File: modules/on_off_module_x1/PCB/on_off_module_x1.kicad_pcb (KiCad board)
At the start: 2 copper layers, 48 x 63 mm, 30 parts, among them J1 Screw_Terminal_01x02, J2 Conn_01x06_Socket, J3 Conn_01x03_Socket, J4 Screw_Terminal_01x02, J5 Screw_Terminal_01x02, K1 12V 5A, Q1 2N7002H, SW1 SW_SPDT, U1 AMS1117-3.3, U2 ESP-12E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

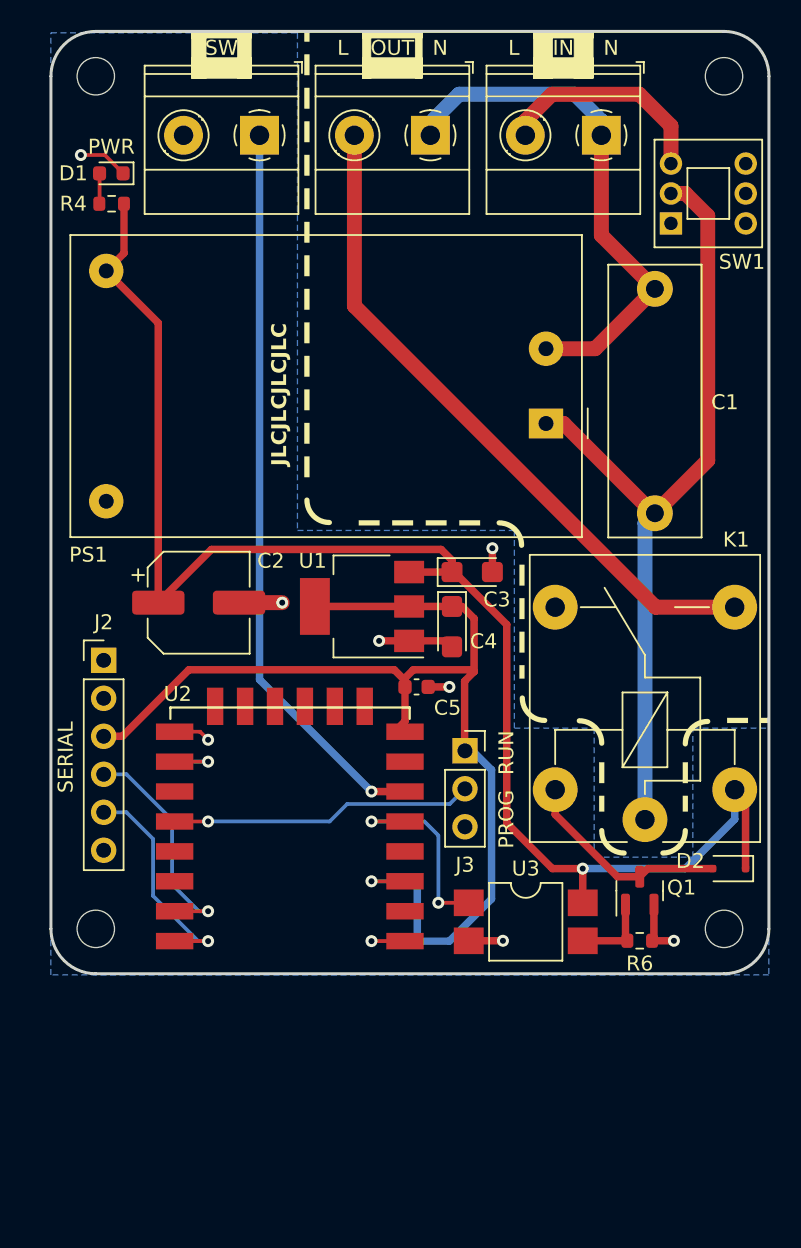
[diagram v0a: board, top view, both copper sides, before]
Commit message: ON-OFF module hardware updated to V2
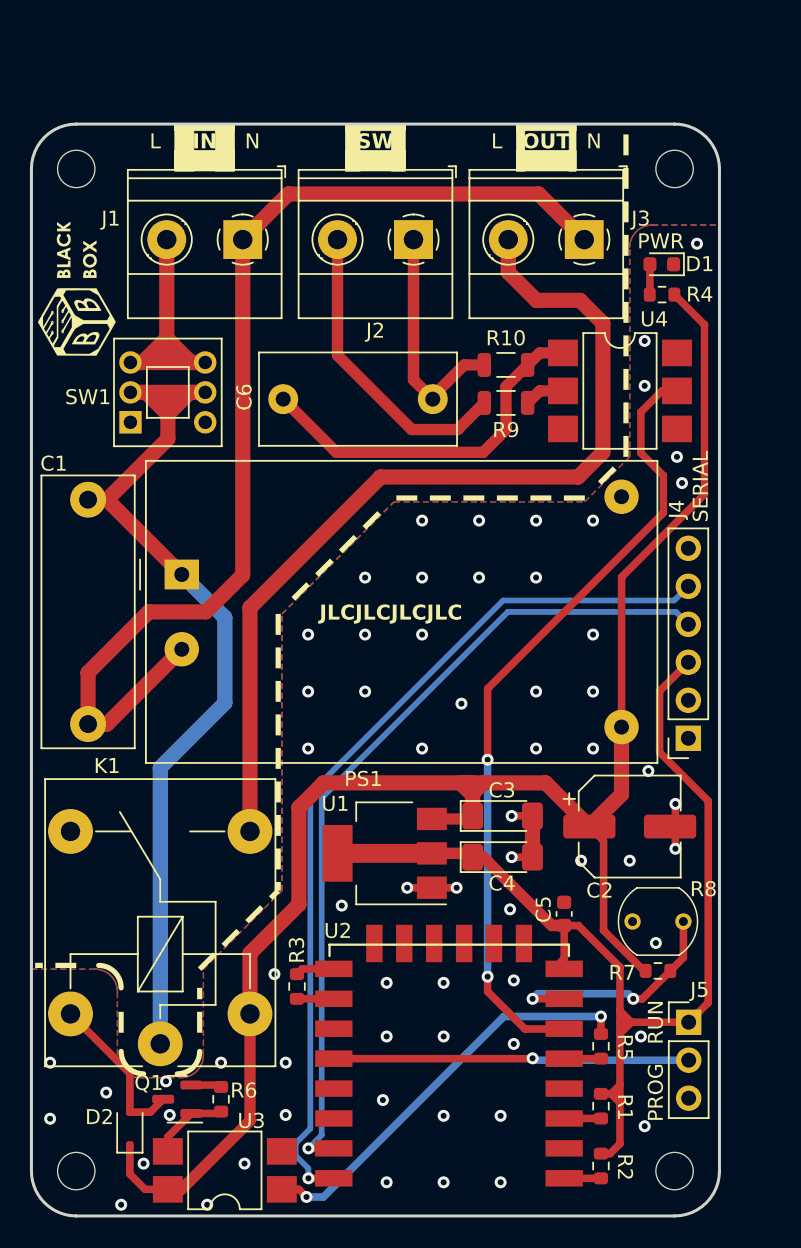
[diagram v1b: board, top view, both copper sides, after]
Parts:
- added C6: 220nF, Alan_Capacitor:CAP_THT_CERAMIC_X2_13x6x12, F.Cu at (152.4, 83.4)
- added G***: LOGO, LOGO, F.Cu at (128.6, 76.1)
- added G***: LOGO, LOGO, B.Cu at (157.0, 123.5)
- added R10: 1M, Alan_Resistor:RES_SMD_1206, F.Cu at (155.8, 81.1)
- added R7: 2.2k, Alan_Resistor:RES_SMD_0603, F.Cu at (166.6, 121.7)
- added R8: 10k, Alan_Sensor:LDR_5_V, F.Cu at (167.4, 118.4)
- added R9: 1k, Alan_Resistor:RES_SMD_1206, F.Cu at (155.8, 83.7)
- added U4: H11AA1, Alan_IC:SMDIP-6_7.62, F.Cu at (164.9, 82.9)
- C1: footprint Capacitor_THT:C_Rect_L18.0mm_W6.0mm_P15.00mm_FKS3_FKP3 -> Alan_Capacitor:CAP_THT_CERAMIC_X2_18x6x15
- C2: footprint Capacitor_SMD:CP_Elec_6.3x7.7 -> Alan_Capacitor:CAP_SMD_ELEC_6.3x7.7
- C3, C4: footprint Capacitor_Tantalum_SMD:CP_EIA-3216-18_Kemet-A -> Alan_Capacitor:CAP_SMD_TANTALUM_CASE-A
- C5: footprint Capacitor_SMD:C_0603_1608Metric -> Alan_Capacitor:CAP_SMD_CERAMIC_0603
- D1: footprint LED_SMD:LED_0603_1608Metric -> Alan_LED:LED_SMD_0603
- D2: footprint Diode_SMD:D_SOD-323F -> Alan_Diode:DIODE_SMD_SOD323F
- J1: footprint TerminalBlock_Phoenix:TerminalBlock_Phoenix_MKDS-1,5-2-5.08_1x02_P5.08mm_Horizontal -> Alan_Connector:CONN_TERMINAL-BLOCK_2P_P5.08
- J2: value Conn_01x06_Socket -> Screw_Terminal_01x02; footprint Connector_PinHeader_2.54mm:PinHeader_1x06_P2.54mm_Vertical -> Alan_Connector:CONN_TERMINAL-BLOCK_2P_P5.08
- J3: value Conn_01x03_Socket -> Screw_Terminal_01x02; footprint Connector_PinSocket_2.54mm:PinSocket_1x03_P2.54mm_Vertical -> Alan_Connector:CONN_TERMINAL-BLOCK_2P_P5.08
- J4: value Screw_Terminal_01x02 -> Conn_01x06_Socket; footprint TerminalBlock_Phoenix:TerminalBlock_Phoenix_MKDS-1,5-2-5.08_1x02_P5.08mm_Horizontal -> Alan_Connector:CONN_SOCKET-HEADER_1x06_V
- J5: value Screw_Terminal_01x02 -> Conn_01x03_Socket; footprint TerminalBlock_Phoenix:TerminalBlock_Phoenix_MKDS-1,5-2-5.08_1x02_P5.08mm_Horizontal -> Alan_Connector:CONN_PIN-HEADER_1x03_V
- K1: footprint Relay_THT:Relay_SPDT_Finder_36.11 -> Alan_Relay:RELAY_SPDT_FINDER_36.11
- PS1: footprint Converter_ACDC:Converter_ACDC_HiLink_HLK-PMxx -> Alan_Module:HILINK_HLK-PMxx
- Q1: footprint Package_TO_SOT_SMD:SOT-23 -> Alan_Transistor:SOT-23
- R1, R2, R3, R5: footprint Resistor_SMD:R_0603_1608Metric -> Alan_Resistor:RES_SMD_0603; moved to F.Cu
- R4, R6: footprint Resistor_SMD:R_0603_1608Metric -> Alan_Resistor:RES_SMD_0603
- SW1: footprint MyLibrary:Toggle_Switch_SelfLocking_7x7 -> Alan_Switches:SW_TOGGLE_DPDT_THT_7x7
- U1: footprint Package_TO_SOT_SMD:SOT-223-3_TabPin2 -> Alan_IC:SOT-223-3_TAB2
- U2: footprint ESP8266:ESP-12E_SMD -> Alan_Module:MOD_ESP-12E
- U3: footprint Package_DIP:SMDIP-4_W7.62mm -> Alan_IC:SMDIP-4_7.62
- moved J5 61.8 mm to (169.5, 125.1), turned to 0 degrees
- moved J4 49.5 mm to (169.5, 106.1)
- moved D2 43.7 mm to (132.1, 132.2), turned to 90 degrees
- moved SW1 38.5 mm to (134.7, 83.0)
- moved R4 38.1 mm to (168.5, 76.4), turned to 180 degrees
- moved C1 37.9 mm to (129.3, 90.1), turned to -90 degrees
- moved D1 37.3 mm to (167.7, 74.4)
- moved K1 35.7 mm to (134.1, 126.5)
- moved J3 35.1 mm to (162.5, 72.8), turned to 180 degrees
- moved J2 34.9 mm to (151.1, 72.8), turned to 180 degrees
- moved Q1 33.9 mm to (135.3, 130.2), turned to 180 degrees
- moved C2 32.5 mm to (165.5, 112.0)
- moved R6 30.2 mm to (138.2, 131.1), turned to 90 degrees
- moved PS1 26.4 mm to (135.6, 95.1), turned to 0 degrees
- moved U3 26.1 mm to (138.5, 135.0), turned to 180 degrees
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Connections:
- C5 pad 1: +3.3V -> GND
- C5 pad 2: GND -> +3.3V
- J2 pad 1: unconnected-(J2-Pin_1-Pad1) -> Net-(J2-Pin_1)
- J2 pad 2: unconnected-(J2-Pin_2-Pad2) -> Net-(J2-Pin_2)
- J3 pad 1: +3.3V -> NEUT
- J3 pad 2: FLASH -> Net-(J3-Pin_2)
- J4 pad 1: SWITCH -> unconnected-(J4-Pin_1-Pad1)
- J4 pad 2: GND -> unconnected-(J4-Pin_2-Pad2)
- J5 pad 1: NEUT -> +3.3V
- J5 pad 2: OUT -> FLASH
- K1 pad 14: OUT -> Net-(J3-Pin_2)
- R4 pad 1: Net-(D1-A) -> +12V
- R4 pad 2: +12V -> Net-(D1-A)
- SW1 pad 4: (no net) -> unconnected-(SW1-A-Pad4)
- SW1 pad 5: (no net) -> LINE
- SW1 pad 6: (no net) -> Net-(J1-Pin_2)
- U2 pad 7: unconnected-(U2-GPIO13-Pad7) -> LDR
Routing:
- net Net-(J3-Pin_2): track 0.00 -> 61.4 mm
- net RX: track 14.3 -> 59.9 mm
- net OUT: track 44.8 -> 0.00 mm
- net TX: track 14.8 -> 56.2 mm
- net NEUT: track 35.4 -> 72.6 mm
- net Net-(C6-Pad2): track 0.00 -> 24.6 mm
- net Net-(J2-Pin_2): track 0.00 -> 20.3 mm
- net Net-(R5-Pad1): track 8.33 -> 27.7 mm, vias 1 -> 2
- net Net-(J2-Pin_1): track 0.00 -> 15.7 mm
- net LDR: track 0.00 -> 15.3 mm, vias 0 -> 2
- net +12V: track 101.3 -> 114.8 mm, vias 1 -> 0
- net LINE: track 55.0 -> 62.8 mm
- net Net-(J1-Pin_2): track 15.1 -> 19.6 mm
- net SWITCH: track 48.3 -> 52.4 mm, vias 1 -> 2
- net GND: track 20.9 -> 17.2 mm, vias 8 -> 65
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- added copper zone on F.Cu, net GND
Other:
- board size 48 x 63 mm -> 46 x 73 mm
- board text removed: "Designed by Alan Carvalho"

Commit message: General files structure refactoring
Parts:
- removed the G*** at (159.0, 80.3)
- removed the J3 at (162.5, 72.8)
- removed J4: Conn_01x06_Socket, Alan_Connector:CONN_SOCKET-HEADER_1x06_V
- removed the REF** at (128.5, 68.0)
- removed SW1: SW_SPDT, Alan_Switches:SW_TOGGLE_DPDT_THT_7x7
- added C7: 100nF, Alan_Capacitor:CAP_SMD_CERAMIC_0603, F.Cu at (168.0, 84.9)
- added F1: 0,25A, Alan_Fuse:FUSEHOLDER_THT_5x20_CLIP, F.Cu at (138.0, 77.9)
- added G***: LOGO, Alan_Label:LABEL_ELECTRIC_SHOCK_RISK_10x10, B.Cu at (144.5, 91.1)
- added L1: 600R, Alan_Inductor:BEAD_SMD_1206, F.Cu at (134.1, 84.3)
- added R11: 33k, Alan_Resistor:RES_SMD_1206, F.Cu at (156.9, 76.1)
- added R12: 10k, Alan_Resistor:RES_SMD_0603, F.Cu at (169.8, 84.1)
- added REF**: MountingHole_3mm_Pad, Alan_Mechanics:MOUNTING_HOLE_PAD_3mm, F.Cu at (128.5, 64.0)
- C6: value 220nF -> 47nF; footprint Alan_Capacitor:CAP_THT_CERAMIC_X2_13x6x12 -> Alan_Capacitor:CAP_THT_CERAMIC_X2_13x5x11_P10
- D2: value 1N4148 -> S1A; footprint Alan_Diode:DIODE_SMD_SOD323F -> Alan_Diode:DIODE_SMD_SMA
- J1: value Screw_Terminal_01x02 -> CONN_TERMINAL-BLOCK_5P_P5.08; footprint Alan_Connector:CONN_TERMINAL-BLOCK_2P_P5.08 -> Alan_Connector:CONN_TERMINAL-BLOCK_5P_P5.08
- J2: value Screw_Terminal_01x02 -> Conn_01x06_Socket; footprint Alan_Connector:CONN_TERMINAL-BLOCK_2P_P5.08 -> Alan_Connector:CONN_SOCKET-HEADER_1x06_V
- R10: value 1M -> 33k
- R4: value 2.2k -> 2k2
- R5: value 390 -> 390R
- R7: value 2.2k -> 33k
- R9: value 1k -> 470k
- moved J2 36.5 mm to (169.5, 104.3)
- moved J1 19.5 mm to (158.7, 68.6)
- moved C6 12.9 mm to (139.5, 84.3), turned to 0 degrees
- moved R10 6.68 mm to (151.5, 76.1)
- moved G*** 6.41 mm to (161.3, 118.7)
- moved G*** 5.33 mm to (130.6, 71.1), turned to 0 degrees
- moved REF** 4.00 mm to (168.5, 64.0)
- moved R9 3.18 mm to (153.4, 85.8), turned to 90 degrees
- moved U4 3.01 mm to (161.9, 82.3)
- moved D2 2.92 mm to (129.8, 130.4), turned to 180 degrees
- moved Q1 2.76 mm to (138.0, 130.2)
- moved R6 2.76 mm to (141.0, 131.1)
- moved D1 2.70 mm to (167.2, 71.8)
- moved R4 2.70 mm to (168.0, 73.8)
- renumbered J5 to J3
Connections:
- C6 pad 1: Net-(J2-Pin_1) -> Net-(C6-Pad1)
- J1 pad 1: NEUT -> Net-(J1-Pin_1)
- J1 pad 2: Net-(J1-Pin_2) -> NEUT
- J2 pad 1: Net-(J2-Pin_1) -> unconnected-(J2-Pin_1-Pad1)
- J2 pad 2: Net-(J2-Pin_2) -> unconnected-(J2-Pin_2-Pad2)
- K1 pad 14: Net-(J3-Pin_2) -> LOAD
- R10 pad 1: Net-(J2-Pin_1) -> NEUT
- R10 pad 2: Net-(C6-Pad2) -> Net-(R10-Pad2)
- R7 pad 1: +12V -> +3.3V
- R9 pad 1: Net-(J2-Pin_2) -> Net-(C6-Pad1)
- R9 pad 2: Net-(R9-Pad2) -> Net-(C6-Pad2)
- U2 pad 15: TX -> UART+
- U2 pad 16: RX -> UART-
- U2 pad 2: unconnected-(U2-ADC-Pad2) -> LDR
- U2 pad 7: LDR -> unconnected-(U2-GPIO13-Pad7)
- U4 pad 2: Net-(R9-Pad2) -> Net-(R11-Pad2)
- U4 pad 5: SWITCH -> Net-(R12-Pad1)
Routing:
- net Net-(J3-Pin_2): track 61.4 -> 0.00 mm
- net UART-: track 0.00 -> 60.5 mm, vias 0 -> 1
- net RX: track 59.9 -> 0.00 mm, vias 1 -> 0
- net UART+: track 0.00 -> 56.4 mm, vias 0 -> 1
- net TX: track 56.2 -> 0.00 mm, vias 1 -> 0
- net LOAD: track 0.00 -> 48.6 mm
- net Net-(C6-Pad1): track 0.00 -> 24.6 mm, vias 0 -> 3
- net Net-(J1-Pin_1): track 0.00 -> 22.5 mm
- net NEUT: track 72.6 -> 50.6 mm
- net SW_IN: track 0.00 -> 21.4 mm
- net Net-(J2-Pin_2): track 20.3 -> 0.00 mm
- net Net-(J1-Pin_2): track 19.6 -> 0.00 mm
- net Net-(J2-Pin_1): track 15.7 -> 0.00 mm
- net Net-(C6-Pad2): track 24.6 -> 10.5 mm
- net Net-(D2-A): track 10.8 -> 20.2 mm, vias 0 -> 1
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- added copper zone on B.Cu, net Earth
- added copper zone on F.Cu, net Earth
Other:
- board size 46 x 73 mm -> 46 x 77 mm
- board text removed: "HV"
- board text removed: "LV"
